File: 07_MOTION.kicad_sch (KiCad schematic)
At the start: 2 parts, among them U2 LSM6DSV16XTR, U3 BMM350

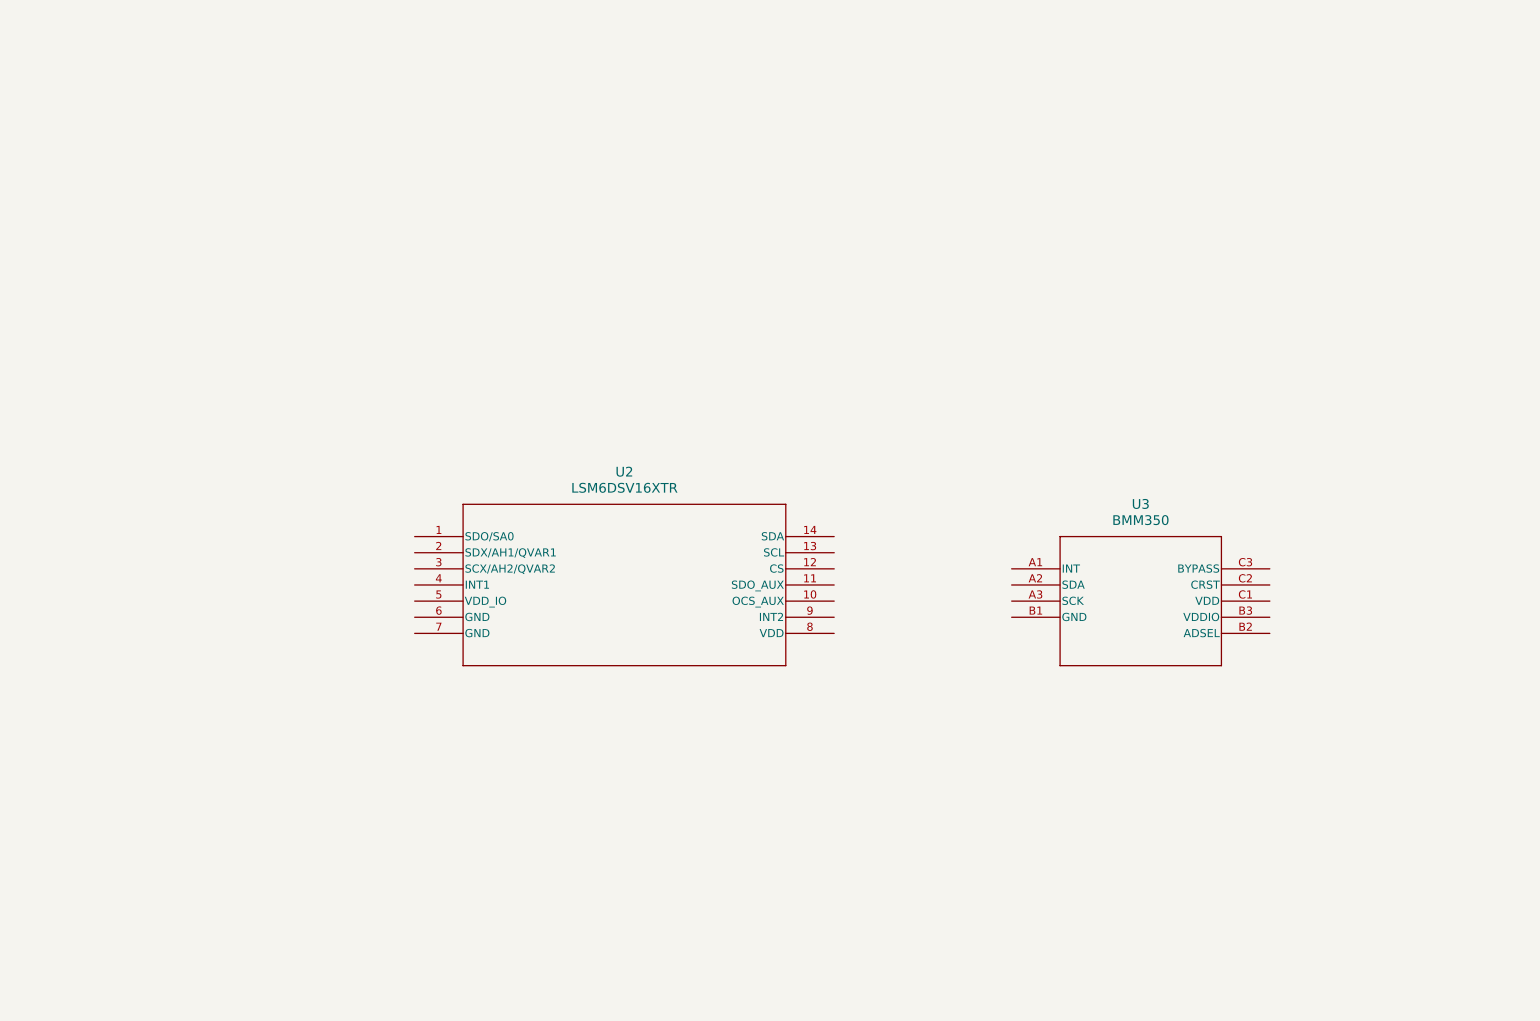
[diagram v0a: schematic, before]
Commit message: updated schematics
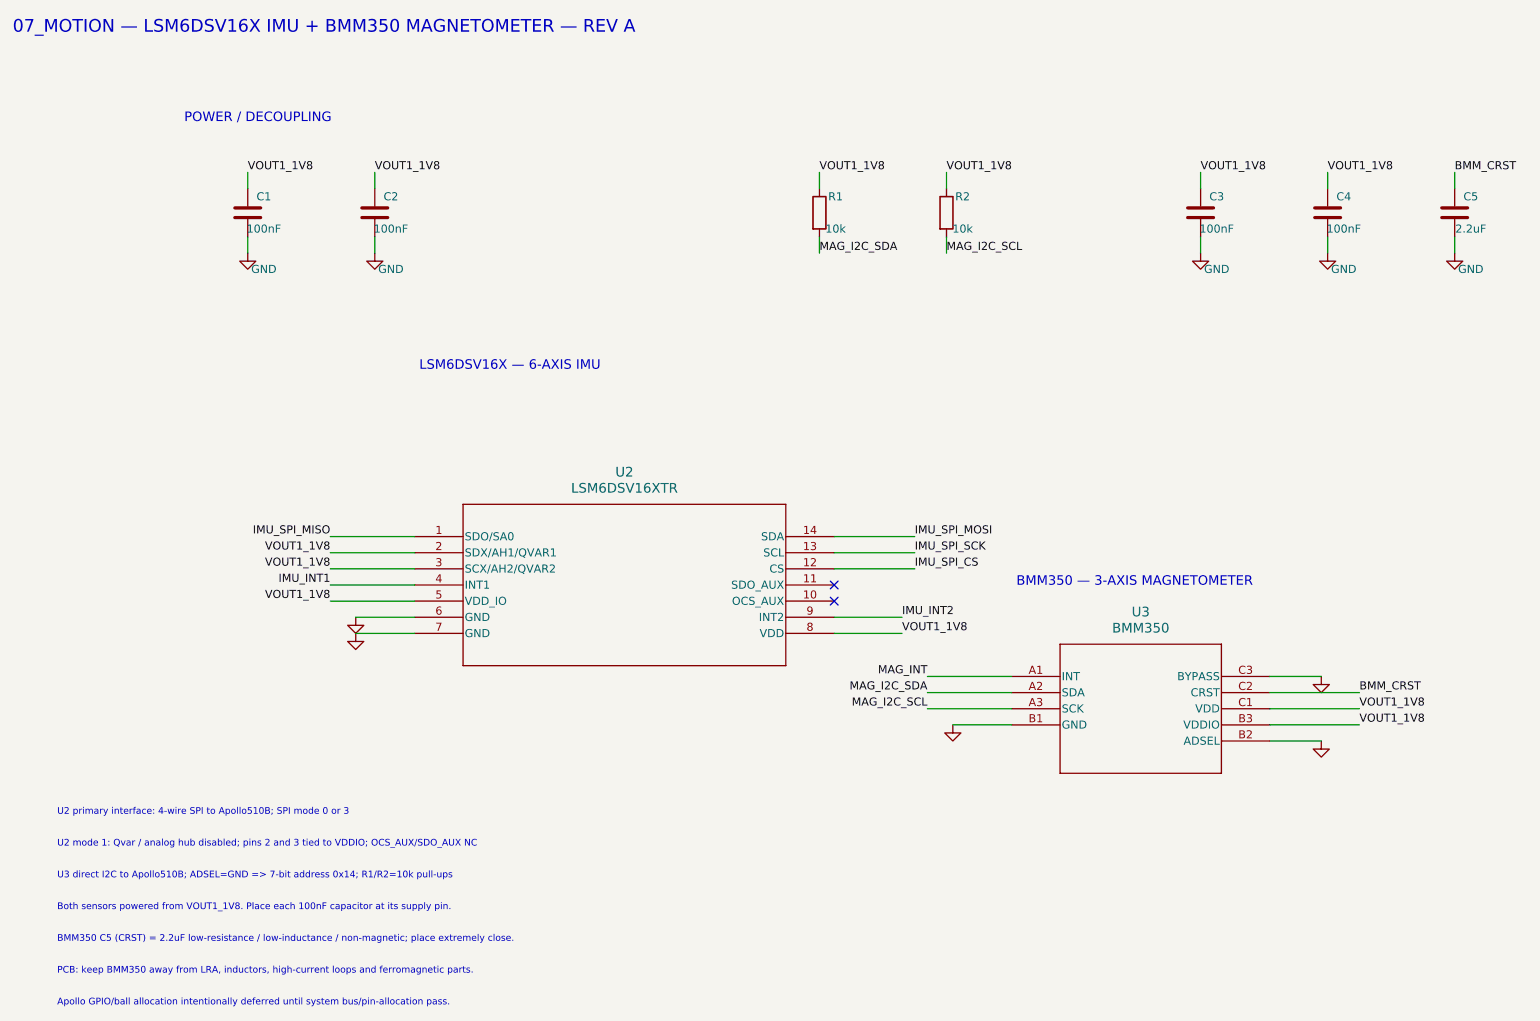
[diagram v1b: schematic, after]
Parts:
- added C1, C2, C3, C4: 100nF, symbol Device:C
- added C5: 2.2uF, symbol Device:C
- added R1, R2: 10k, symbol Device:R
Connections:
- net MAG_INT: now reaches U3.A1 (INT)
- net MAG_I2C_SDA: now reaches U3.A2 (SDA)
- net MAG_I2C_SDA: now also R1.2
- net MAG_I2C_SCL: now reaches U3.A3 (SCK)
- net MAG_I2C_SCL: now also R2.2
- net GND: now reaches U3.B1 (GND)
- net GND: now also U2.6 (GND), U2.7 (GND), U3.B2 (ADSEL), U3.C3 (BYPASS), C1.2, C2.2, C3.2, C4.2, C5.2
- net VOUT1_1V8: now reaches U3.B3 (VDDIO)
- net VOUT1_1V8: now also U2.2 (SDX/AH1/QVAR1), U2.3 (SCX/AH2/QVAR2), U2.5 (VDD_IO), U2.8 (VDD), U3.C1 (VDD), C1.1, C2.1, C3.1, C4.1, R1.1, R2.1
- net BMM_CRST: now reaches U3.C2 (CRST)
- net BMM_CRST: now also C5.1
- net IMU_SPI_MISO: now reaches U2.1 (SDO/SA0)
- net IMU_SPI_CS: now reaches U2.12 (CS)
- net IMU_SPI_SCK: now reaches U2.13 (SCL)
- net IMU_SPI_MOSI: now reaches U2.14 (SDA)
- net IMU_INT1: now reaches U2.4 (INT1)
- net IMU_INT2: now reaches U2.9 (INT2)
- no-connect marks 0 -> 2
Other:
- note added: "07_MOTION — LSM6DSV16X IMU + BMM350 MAGNETOMETER — REV A"
- note added: "Apollo GPIO/ball allocation intentionally deferred until system bus/pin-allocation pass."
- note added: "BMM350 C5 (CRST) = 2.2uF low-resistance / low-inductance / non-magnetic; place extremely close."
- note added: "BMM350 — 3-AXIS MAGNETOMETER"
- note added: "Both sensors powered from VOUT1_1V8. Place each 100nF capacitor at its supply pin."
- note added: "LSM6DSV16X — 6-AXIS IMU"
- note added: "PCB: keep BMM350 away from LRA, inductors, high-current loops and ferromagnetic parts."
- note added: "POWER / DECOUPLING"
- note added: "U2 mode 1: Qvar / analog hub disabled; pins 2 and 3 tied to VDDIO; OCS_AUX/SDO_AUX NC"
- note added: "U2 primary interface: 4-wire SPI to Apollo510B; SPI mode 0 or 3"
- note added: "U3 direct I2C to Apollo510B; ADSEL=GND => 7-bit address 0x14; R1/R2=10k pull-ups"
- moved on the sheet: U3

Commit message: refactor(kicad): integrate Rev-A hierarchy and libraries
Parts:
- renumbered C1 to C701, C2 to C702, C3 to C703, C4 to C704, C5 to C705, R1 to R701, R2 to R702, U2 to U702, U3 to U703
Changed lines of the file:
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@@
 		)
 	)
-	(label "VOUT1_1V8"
+	(hierarchical_label "VOUT1_1V8"
+		(shape passive)
 		(at 230 123.62 0)
 		(effects
@@
 		)
 	)
-	(label "IMU_SPI_CS"
+	(hierarchical_label "IMU_SPI_CS"
+		(shape input)
 		(at 160 99.06 0)
 		(effects
@@
 		)
 	)
-	(label "IMU_SPI_MISO"
+	(hierarchical_label "IMU_SPI_MISO"
+		(shape output)
 		(at 68 93.98 180)
 		(effects
@@
 		)
 	)
-	(label "IMU_INT2"
+	(hierarchical_label "IMU_INT2"
+		(shape output)
 		(at 158 106.68 0)
 		(effects
@@
 		)
 	)
-	(label "MAG_I2C_SCL"
+	(hierarchical_label "MAG_I2C_SCL"
+		(shape bidirectional)
 		(at 162 121.08 180)
 		(effects
@@
 		)
 	)
-	(label "IMU_INT1"
+	(hierarchical_label "IMU_INT1"
+		(shape output)
 		(at 68 101.6 180)
 		(effects
@@
 		)
 	)
-	(label "MAG_I2C_SDA"
+	(hierarchical_label "MAG_I2C_SDA"
+		(shape bidirectional)
 		(at 145 49.35 0)
 		(effects
@@
 		)
 	)
-	(label "IMU_SPI_MOSI"
+	(hierarchical_label "IMU_SPI_MOSI"
+		(shape input)
 		(at 160 93.98 0)
 		(effects
@@
 		)
 	)
-	(label "IMU_SPI_SCK"
+	(hierarchical_label "IMU_SPI_SCK"
+		(shape input)
 		(at 160 96.52 0)
 		(effects
@@
 		)
 	)
-	(label "MAG_INT"
+	(hierarchical_label "MAG_INT"
+		(shape output)
 		(at 162 116 180)
 		(effects
@@
 		(dnp no)
 		(fields_autoplaced yes)
-		(property "Reference" "R2"
+		(property "Reference" "R702"
 			(at 167.54 40.46 0)
 			(show_name no)
@@
 			(project "sportwatch_revA"
 				(path "/063f9d99-6c07-44cf-ba32-e33897e06972/0fde0b30-f543-4029-8455-03e39821fc60"
-					(reference "R2")
+					(reference "R702")
 					(unit 1)
 				)
@@
 		(dnp no)
 		(fields_autoplaced yes)
-		(property "Reference" "C3"
+		(property "Reference" "C703"
 			(at 207.54 40.46 0)
 			(show_name no)
@@
 			(project "sportwatch_revA"
 				(path "/063f9d99-6c07-44cf-ba32-e33897e06972/0fde0b30-f543-4029-8455-03e39821fc60"
-					(reference "C3")
+					(reference "C703")
 					(unit 1)
 				)
@@
 		(dnp no)
 		(fields_autoplaced yes)
-		(property "Reference" "U3"
+		(property "Reference" "U703"
 			(at 195.58 105.84 0)
 			(show_name no)
@@
 			(project "sportwatch_revA"
 				(path "/063f9d99-6c07-44cf-ba32-e33897e06972/0fde0b30-f543-4029-8455-03e39821fc60"
-					(reference "U3")
+					(reference "U703")
 					(unit 1)
 				)
@@
 		(dnp no)
 		(fields_autoplaced yes)
-		(property "Reference" "C4"
+		(property "Reference" "C704"
 			(at 227.54 40.46 0)
 			(show_name no)
@@
 			(project "sportwatch_revA"
 				(path "/063f9d99-6c07-44cf-ba32-e33897e06972/0fde0b30-f543-4029-8455-03e39821fc60"
-					(reference "C4")
+					(reference "C704")
 					(unit 1)
 				)
@@
 		(dnp no)
 		(fields_autoplaced yes)
-		(property "Reference" "R1"
+		(property "Reference" "R701"
 			(at 147.54 40.46 0)
 			(show_name no)
@@
 			(project "sportwatch_revA"
 				(path "/063f9d99-6c07-44cf-ba32-e33897e06972/0fde0b30-f543-4029-8455-03e39821fc60"
-					(reference "R1")
+					(reference "R701")
 					(unit 1)
 				)
@@
 		(dnp no)
 		(fields_autoplaced yes)
-		(property "Reference" "C2"
+		(property "Reference" "C702"
 			(at 77.54 40.46 0)
 			(show_name no)
@@
 			(project "sportwatch_revA"
 				(path "/063f9d99-6c07-44cf-ba32-e33897e06972/0fde0b30-f543-4029-8455-03e39821fc60"
-					(reference "C2")
+					(reference "C702")
 					(unit 1)
 				)
@@
 		(dnp no)
 		(fields_autoplaced yes)
-		(property "Reference" "C1"
+		(property "Reference" "C701"
 			(at 57.54 40.46 0)
 			(show_name no)
@@
 			(project "sportwatch_revA"
 				(path "/063f9d99-6c07-44cf-ba32-e33897e06972/0fde0b30-f543-4029-8455-03e39821fc60"
-					(reference "C1")
+					(reference "C701")
 					(unit 1)
 				)
@@
 		(dnp no)
 		(fields_autoplaced yes)
-		(property "Reference" "C5"
+		(property "Reference" "C705"
 			(at 247.54 40.46 0)
 			(show_name no)
@@
 			(project "sportwatch_revA"
 				(path "/063f9d99-6c07-44cf-ba32-e33897e06972/0fde0b30-f543-4029-8455-03e39821fc60"
-					(reference "C5")
+					(reference "C705")
 					(unit 1)
 				)
@@
 		(dnp no)
 		(fields_autoplaced yes)
-		(property "Reference" "U2"
+		(property "Reference" "U702"
 			(at 114.3 83.82 0)
 			(show_name no)
@@
 			(project "sportwatch_revA"
 				(path "/063f9d99-6c07-44cf-ba32-e33897e06972/0fde0b30-f543-4029-8455-03e39821fc60"
-					(reference "U2")
+					(reference "U702")
 					(unit 1)
 				)

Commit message: feat(kicad): assign and audit Rev-A footprints
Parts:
- C701, C702, C703, C704: footprint (none) -> Capacitor_SMD:C_0402_1005Metric
- C705: footprint (none) -> Capacitor_SMD:C_0805_2012Metric
- R701, R702: footprint (none) -> Resistor_SMD:R_0402_1005Metric
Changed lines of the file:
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@@
 			)
 		)
-		(property "Footprint" ""
+		(property "Footprint" "Resistor_SMD:R_0402_1005Metric"
 			(at 165 43 0)
 			(hide yes)
@@
 			)
 		)
-		(property "Footprint" ""
+		(property "Footprint" "Capacitor_SMD:C_0402_1005Metric"
 			(at 205 43 0)
 			(hide yes)
@@
 			)
 		)
-		(property "Footprint" ""
+		(property "Footprint" "Capacitor_SMD:C_0402_1005Metric"
 			(at 225 43 0)
 			(hide yes)
@@
 			)
 		)
-		(property "Footprint" ""
+		(property "Footprint" "Resistor_SMD:R_0402_1005Metric"
 			(at 145 43 0)
 			(hide yes)
@@
 			)
 		)
-		(property "Footprint" ""
+		(property "Footprint" "Capacitor_SMD:C_0402_1005Metric"
 			(at 75 43 0)
 			(hide yes)
@@
 			)
 		)
-		(property "Footprint" ""
+		(property "Footprint" "Capacitor_SMD:C_0402_1005Metric"
 			(at 55 43 0)
 			(hide yes)
@@
 			)
 		)
-		(property "Footprint" ""
+		(property "Footprint" "Capacitor_SMD:C_0805_2012Metric"
 			(at 245 43 0)
 			(hide yes)

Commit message: foundation correction
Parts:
- C701, C702, C703, C704, C705, R701, R702, U702, U703: Board (none) -> MAIN
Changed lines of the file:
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@@
 			)
 		)
-	)
+(property "Board" "MAIN" (at 0 0 0) (effects (font (size 1 1)) (hide yes)))
+)
 	(symbol
 		(lib_id "Device:C")
@@
 			)
 		)
-	)
+(property "Board" "MAIN" (at 0 0 0) (effects (font (size 1 1)) (hide yes)))
+)
 	(symbol
 		(lib_id "power:GND")
@@
 			)
 		)
-	)
+(property "Board" "MAIN" (at 0 0 0) (effects (font (size 1 1)) (hide yes)))
+)
 	(symbol
 		(lib_id "power:GND")
@@
 			)
 		)
-	)
+(property "Board" "MAIN" (at 0 0 0) (effects (font (size 1 1)) (hide yes)))
+)
 	(symbol
 		(lib_id "sportwatch_bmm350:BMM350")
@@
 			)
 		)
-	)
+(property "Board" "MAIN" (at 0 0 0) (effects (font (size 1 1)) (hide yes)))
+)
 	(symbol
 		(lib_id "Device:C")
@@
 			)
 		)
-	)
+(property "Board" "MAIN" (at 0 0 0) (effects (font (size 1 1)) (hide yes)))
+)
 	(symbol
 		(lib_id "power:GND")
@@
 			)
 		)
-	)
+(property "Board" "MAIN" (at 0 0 0) (effects (font (size 1 1)) (hide yes)))
+)
 	(symbol
 		(lib_id "power:GND")
@@
 			)
 		)
-	)
+(property "Board" "MAIN" (at 0 0 0) (effects (font (size 1 1)) (hide yes)))
+)
 	(symbol
 		(lib_id "Device:R")
@@
 			)
 		)
-	)
+(property "Board" "MAIN" (at 0 0 0) (effects (font (size 1 1)) (hide yes)))
+)
 	(symbol
 		(lib_id "Device:C")
@@
 			)
 		)
-	)
+(property "Board" "MAIN" (at 0 0 0) (effects (font (size 1 1)) (hide yes)))
+)
 	(symbol
 		(lib_id "Device:C")
@@
 			)
 		)
-	)
+(property "Board" "MAIN" (at 0 0 0) (effects (font (size 1 1)) (hide yes)))
+)
 	(symbol
 		(lib_id "power:GND")
@@
 			)
 		)
-	)
+(property "Board" "MAIN" (at 0 0 0) (effects (font (size 1 1)) (hide yes)))
+)
 	(symbol
 		(lib_id "power:GND")
@@
 			)
 		)
-	)
+(property "Board" "MAIN" (at 0 0 0) (effects (font (size 1 1)) (hide yes)))
+)
 	(symbol
 		(lib_id "power:GND")
@@
 			)
 		)
-	)
+(property "Board" "MAIN" (at 0 0 0) (effects (font (size 1 1)) (hide yes)))
+)
 	(symbol
 		(lib_id "Device:C")
@@
 			)
 		)
-	)
+(property "Board" "MAIN" (at 0 0 0) (effects (font (size 1 1)) (hide yes)))
+)
 	(symbol
 		(lib_id "sportwatch_lsm6dsv16x:LSM6DSV16XTR")
@@
 			)
 		)
-	)
+(property "Board" "MAIN" (at 0 0 0) (effects (font (size 1 1)) (hide yes)))
+)
 	(symbol
 		(lib_id "power:GND")
@@
 			)
 		)
-	)
+(property "Board" "MAIN" (at 0 0 0) (effects (font (size 1 1)) (hide yes)))
+)
 	(symbol
 		(lib_id "power:GND")
@@
 			)
 		)
-	)
+(property "Board" "MAIN" (at 0 0 0) (effects (font (size 1 1)) (hide yes)))
+)
 	(symbol
 		(lib_id "power:GND")
@@
 			)
 		)
-	)
-)
+(property "Board" "MAIN" (at 0 0 0) (effects (font (size 1 1)) (hide yes)))
+)
+)
